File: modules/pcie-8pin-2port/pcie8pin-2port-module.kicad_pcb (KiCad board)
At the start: 4 copper layers, 105.7 x 66 mm, 24 parts, among them J1 RJ45_Amphenol_54602-x08_Horiz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, J5 USB_C_Receptacle_XKB_U262-16X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, SW1 Panasonic_EVQPUJ_EVQPUA, SW2 Panasonic_EVQPUJ_EVQPUA, U1 ESP32-S2-MINI-1, U10 VSSOP-10_3x3mm_P0.5mm, U11 VSSOP-10_3x3mm_P0.5mm, U2 SOIC-8_3.9x4.9mm_P1.27mm, U3 SOT-23-5

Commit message: PCIe: split into 2-port/3-port SKUs; generalize PCB gen; fix mount overlap
Per review: connectors were overlapping the corner mounts, and PCIe needs SKU
separation into a 2-port (4 connectors) and 3-port (6 connectors) board.

PCIe SKU separation:
- gen-modules.py SENSE/MODS now build pcie-8pin-2port (2 cables) and
  pcie-8pin-3port (3 cables); PINMAP keyed off the pcie base.
- modules/pcie-8pin renamed to modules/pcie-8pin-3port (git mv, history kept);
  new modules/pcie-8pin-2port added. Both schematics generated + audit-clean.

Generalized PCB floorplan generator (scripts/gen-module-pcb.py, replaces the
EPS-only gen-eps-pcb.py): parametric in cable count N. Generates EPS (2 cables,
~106x66), PCIe-2port (2, ~106x66) and PCIe-3port (3, ~133x66). N cables inline
(IN top / OUT bottom), cables INSET so the four corner M3 mounts clear the
connectors; shunts moved to mid-gap; the ESP + flash front end + RJ-45 vertically
separated on the right. Verified: 0 shorting_items on all three (was 8-10);
remaining DRC (~33 EPS / ~42 3-port) is silk/placement refinement for the GUI.

CLAUDE.md (board table, layout, generator bullet) + module READMEs updated.
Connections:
- J_IN1 pad 4: /SENSEC1_HI -> GND
- J_IN2 pad 4: /SENSEC2_HI -> GND
- J_OUT1 pad 4: /SENSEC1_LO -> GND
- J_OUT2 pad 4: /SENSEC2_LO -> GND
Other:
- board text added: "CEC pcie8pin-2port-module 4L 2oz/1oz"
- board text removed: "CEC eps8pin-module 4L 2oz/1oz"
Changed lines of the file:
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@@
 	)
 	(pad "4" thru_hole oval (at 12.6 0) (size 2.7 3.7) (drill 1.8) (layers "*.Cu" "*.Mask") (remove_unused_layers no)
-		(net 13 "/SENSEC1_HI")
+		(net 22 "GND")
 	)
 	(pad "5" thru_hole oval (at 0 5.5) (size 2.7 3.7) (drill 1.8) (layers "*.Cu" "*.Mask") (remove_unused_layers no)
@@
 	)
 	(pad "4" thru_hole oval (at 12.6 0) (size 2.7 3.7) (drill 1.8) (layers "*.Cu" "*.Mask") (remove_unused_layers no)
-		(net 14 "/SENSEC1_LO")
+		(net 22 "GND")
 	)
 	(pad "5" thru_hole oval (at 0 5.5) (size 2.7 3.7) (drill 1.8) (layers "*.Cu" "*.Mask") (remove_unused_layers no)
@@
 	)
 	(pad "4" thru_hole oval (at 12.6 0) (size 2.7 3.7) (drill 1.8) (layers "*.Cu" "*.Mask") (remove_unused_layers no)
-		(net 15 "/SENSEC2_HI")
+		(net 22 "GND")
 	)
 	(pad "5" thru_hole oval (at 0 5.5) (size 2.7 3.7) (drill 1.8) (layers "*.Cu" "*.Mask") (remove_unused_layers no)
@@
 	)
 	(pad "4" thru_hole oval (at 12.6 0) (size 2.7 3.7) (drill 1.8) (layers "*.Cu" "*.Mask") (remove_unused_layers no)
-		(net 16 "/SENSEC2_LO")
+		(net 22 "GND")
 	)
 	(pad "5" thru_hole oval (at 0 5.5) (size 2.7 3.7) (drill 1.8) (layers "*.Cu" "*.Mask") (remove_unused_layers no)
@@
 	(gr_line (start 105.7 66) (end 0 66) (stroke (width 0.1) (type solid)) (layer "Edge.Cuts"))
 	(gr_line (start 0 66) (end 0 0) (stroke (width 0.1) (type solid)) (layer "Edge.Cuts"))
-	(gr_text "CEC eps8pin-module  4L 2oz/1oz" (at 39.8 62 0) (layer "B.SilkS") (effects (font (size 0.9 0.9) (thickness 0.13)) (justify mirror)))
+	(gr_text "CEC pcie8pin-2port-module  4L 2oz/1oz" (at 39.8 62 0) (layer "B.SilkS") (effects (font (size 0.9 0.9) (thickness 0.13)) (justify mirror)))
 	(embedded_fonts no)
 )

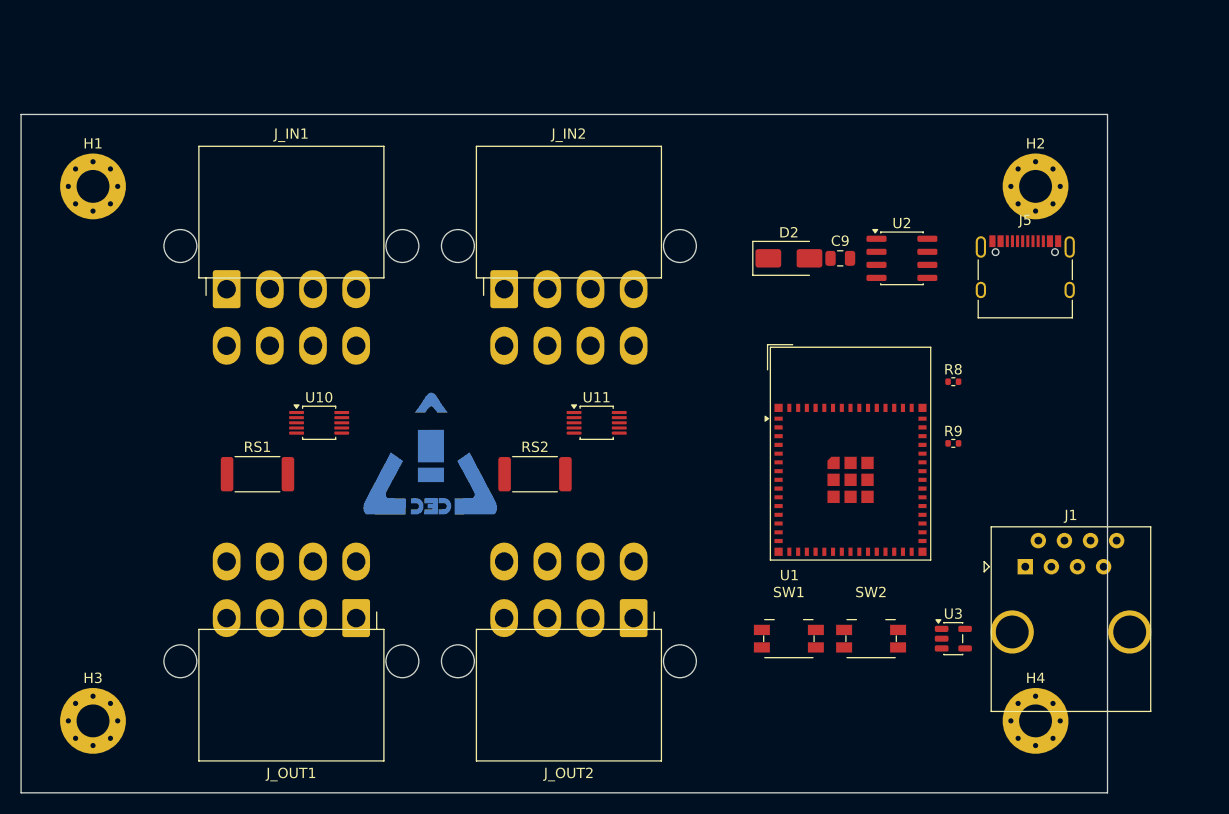
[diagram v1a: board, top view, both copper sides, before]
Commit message: Rotate USB-C + RJ-45 to mate outward on the right edge
Per review: the right-edge connectors (USB-C J5, RJ-45 J1) were mating downward
(+Y) instead of outward. Both footprints' openings face +Y at rotation 0, so
rotate them 90 (KiCad CCW, +Y -> +X) to mate out the right edge. The rotated
RJ-45 is ~18mm deep, so widen the electronics region (W = ex+40) and re-place
the core/flash around it; boards are now ~110x66 (EPS, PCIe-2port) and ~137x66
(PCIe-3port).

gen-module-pcb.py now bakes the footprint rotation into each pad's angle field
(KiCad convention). Without it, kicad-cli's headless DRC reported 25 FALSE
within-footprint pad shorts on the rotated USB-C (a known artifact, GUI-clean,
0 cross-part); with it, all three boards are back to 0 shorting_items,
0 clearance, 0 pth-in-courtyard (total DRC ~22 EPS / ~30 3-port, just silk).

CLAUDE.md + module READMEs updated (board sizes, connector orientation).
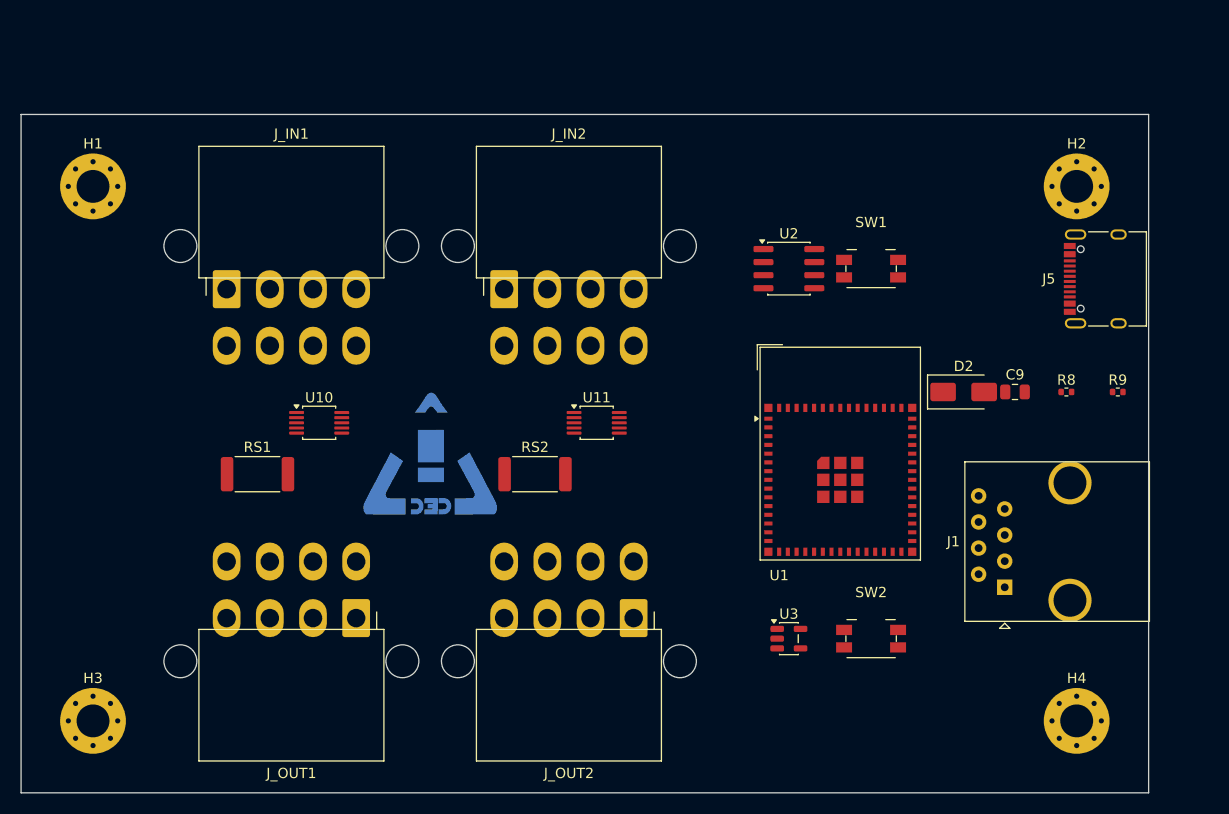
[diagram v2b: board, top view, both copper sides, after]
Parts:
- moved SW1 36.9 mm to (82.7, 15.0)
- moved C9 21.4 mm to (96.7, 27.0)
- moved D2 21.4 mm to (91.7, 27.0)
- moved R9 16.8 mm to (106.7, 27.0)
- moved U3 16.0 mm to (74.7, 51.0)
- moved R8 11.0 mm to (101.7, 27.0)
- moved U2 11.0 mm to (74.7, 15.0)
- moved J5 8.00 mm to (105.7, 16.0), turned to 90 degrees
- moved H2 4.00 mm to (102.7, 7.00)
- moved H4 4.00 mm to (102.7, 59.0)
- moved J1 2.83 mm to (95.7, 46.0), turned to 90 degrees
- moved U1 1.00 mm to (79.7, 33.0)
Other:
- board size 105.7 x 66 mm -> 109.7 x 66 mm

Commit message: 12VHPWR Standard: add INA240 input RC filter, sideband sense taps, tighten board + values-on-silk
Schematic (gen-modules.py, analog-pin topology):
- INA240 input anti-alias/transient RC filter per channel: matched 10 ohm series
  Rf on each input (RFH/RFL1-6) + 470 nF differential cap (CF1-6).
  fc = 1/(2*pi*2*Rf*Cdiff) ~= 16.9 kHz, so the ~10 kHz GPU transients pass at
  ~-1.3 dB and HF rolls off ahead of the ESP32-S3 ADC. Rf held at 10 ohm + matched
  (TI's INA240 ceiling) for negligible gain/CMRR error.
- The four 12V-2x6 sideband sense pins (13-16: SENSE0/SENSE1/CARD_PWR_STABLE/
  CARD_CBL_PRES#) now pass through J3->J4 AND each taps a free ESP32-S3 GPIO
  (IO8/9/11/12) via a 1k series R (R10-R13) so firmware can read the cable's
  advertised power capability + present/stable state and report over CAN.
- Moved the I2C pull-ups R3/R4 into the i2c-only branch (they were unused/floating
  on the analog module) to free IO8/IO9 for two of the sideband taps.
- footprint_for: 470n -> C_0603. ERC clean; netlist verified.

PCB floorplan (gen-module-pcb.py):
- Values-on-silk pass (all boards): place() rewrites each part's Value property to
  the netlist value and moves it from the non-plotted F.Fab to F.SilkS so values
  are readable on the board; mounts/logo keep their Fab default.
- 12VHPWR tightened 46x104 -> 44x92 with plug connectors overhanging their edge:
  J3's right-angle shroud overhangs the TOP edge (~3mm, pads ~6.5mm in), J1/J5
  overhang the RIGHT edge; J4 keeps J3's rotation so the six +12V lanes stay
  straight + equal-length (melt prevention). Shunt rows spaced 8mm (rotated 2512
  is 6.3mm tall), mounts moved above/below the 14mm ESP.
- DRC: 0 structural hits (0 copper shorts / clearance / courtyard / copper-edge);
  remaining is silk (values-on-silk + tight placement) + known lib_footprint_mismatch.

Docs: README + CLAUDE.md updated to match.
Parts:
- C9: value C_0805_2012Metric -> 10uF
- D2: value D_SMA -> SS34
- J1: value RJ45_Amphenol_54602-x08_Horizontal -> TO-HUB
- J5: value USB_C_Receptacle_XKB_U262-16XN-4BVC11 -> USB-C 2.0
- J_IN1: value Molex_Mini-Fit_Jr_5569-08A2_2x04_P4.20mm_Horizontal -> C1 PSU
- J_IN2: value Molex_Mini-Fit_Jr_5569-08A2_2x04_P4.20mm_Horizontal -> C2 PSU
- J_OUT1: value Molex_Mini-Fit_Jr_5569-08A2_2x04_P4.20mm_Horizontal -> C1 LOAD
- J_OUT2: value Molex_Mini-Fit_Jr_5569-08A2_2x04_P4.20mm_Horizontal -> C2 LOAD
- R8, R9: value R_0402_1005Metric -> 5.1kΩ
- RS1, RS2: value R_2512_6332Metric -> 0.5mΩ
- SW1: value Panasonic_EVQPUJ_EVQPUA -> BOOT
- SW2: value Panasonic_EVQPUJ_EVQPUA -> RESET
- U1: value ESP32-S2-MINI-1 -> ESP32-S3-MINI-1-N4R2
- U10, U11: value VSSOP-10_3x3mm_P0.5mm -> INA238
- U2: value SOIC-8_3.9x4.9mm_P1.27mm -> TJA1462A
- U3: value SOT-23-5 -> LP5907MFX-3.3
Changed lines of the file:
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@@
 		(effects (font (size 1 1) (thickness 0.15)))
 	)
-	(property "Value" "Molex_Mini-Fit_Jr_5569-08A2_2x04_P4.20mm_Horizontal"
+	(property "Value" "C1 PSU"
 		(at 6.3 8.55 0)
-		(layer "F.Fab")
+		(layer "F.SilkS")
 		(effects (font (size 1 1) (thickness 0.15)))
 	)
@@
 		(effects (font (size 1 1) (thickness 0.15)))
 	)
-	(property "Value" "Molex_Mini-Fit_Jr_5569-08A2_2x04_P4.20mm_Horizontal"
+	(property "Value" "C1 LOAD"
 		(at 6.3 8.55 0)
-		(layer "F.Fab")
+		(layer "F.SilkS")
 		(effects (font (size 1 1) (thickness 0.15)))
 	)
@@
 		)
 	)
-	(property "Value" "R_2512_6332Metric"
+	(property "Value" "0.5mΩ"
 		(at 0 2.63 0)
-		(layer "F.Fab")
+		(layer "F.SilkS")
 		(effects
 			(font
@@
 		)
 	)
-	(property "Value" "VSSOP-10_3x3mm_P0.5mm"
+	(property "Value" "INA238"
 		(at 0 2.45 0)
-		(layer "F.Fab")
+		(layer "F.SilkS")
 		(effects
 			(font
@@
 		(effects (font (size 1 1) (thickness 0.15)))
 	)
-	(property "Value" "Molex_Mini-Fit_Jr_5569-08A2_2x04_P4.20mm_Horizontal"
+	(property "Value" "C2 PSU"
 		(at 6.3 8.55 0)
-		(layer "F.Fab")
+		(layer "F.SilkS")
 		(effects (font (size 1 1) (thickness 0.15)))
 	)
@@
 		(effects (font (size 1 1) (thickness 0.15)))
 	)
-	(property "Value" "Molex_Mini-Fit_Jr_5569-08A2_2x04_P4.20mm_Horizontal"
+	(property "Value" "C2 LOAD"
 		(at 6.3 8.55 0)
-		(layer "F.Fab")
+		(layer "F.SilkS")
 		(effects (font (size 1 1) (thickness 0.15)))
 	)
@@
 		)
 	)
-	(property "Value" "R_2512_6332Metric"
+	(property "Value" "0.5mΩ"
 		(at 0 2.63 0)
-		(layer "F.Fab")
+		(layer "F.SilkS")
 		(effects
 			(font
@@
 		)
 	)
-	(property "Value" "VSSOP-10_3x3mm_P0.5mm"
+	(property "Value" "INA238"
 		(at 0 2.45 0)
-		(layer "F.Fab")
+		(layer "F.SilkS")
 		(effects
 			(font
@@
 		)
 	)
-	(property "Value" "ESP32-S2-MINI-1"
+	(property "Value" "ESP32-S3-MINI-1-N4R2"
 		(at 0 3.55 0)
 		(unlocked yes)
-		(layer "F.Fab")
+		(layer "F.SilkS")
 		(effects
 			(font
@@
 		)
 	)
-	(property "Value" "SOIC-8_3.9x4.9mm_P1.27mm"
+	(property "Value" "TJA1462A"
 		(at 0 3.4 0)
-		(layer "F.Fab")
+		(layer "F.SilkS")
 		(effects
 			(font
@@
 		)
 	)
-	(property "Value" "SOT-23-5"
+	(property "Value" "LP5907MFX-3.3"
 		(at 0 2.4 0)
-		(layer "F.Fab")
+		(layer "F.SilkS")
 		(effects
 			(font
@@
 		)
 	)
-	(property "Value" "Panasonic_EVQPUJ_EVQPUA"
+	(property "Value" "BOOT"
 		(at 0 3.5 0)
-		(layer "F.Fab")
+		(layer "F.SilkS")
 		(effects
 			(font
@@
 		)
 	)
-	(property "Value" "Panasonic_EVQPUJ_EVQPUA"
+	(property "Value" "RESET"
 		(at 0 3.5 0)
-		(layer "F.Fab")
+		(layer "F.SilkS")
 		(effects
 			(font
@@
 		)
 	)
-	(property "Value" "D_SMA"
+	(property "Value" "SS34"
 		(at 0 2.6 0)
-		(layer "F.Fab")
+		(layer "F.SilkS")
 		(effects
 			(font
@@
 		)
 	)
-	(property "Value" "C_0805_2012Metric"
+	(property "Value" "10uF"
 		(at 0 1.68 0)
-		(layer "F.Fab")
+		(layer "F.SilkS")
 		(effects
 			(font
@@
 		)
 	)
-	(property "Value" "R_0402_1005Metric"
+	(property "Value" "5.1kΩ"
 		(at 0 1.17 0)
-		(layer "F.Fab")
+		(layer "F.SilkS")
 		(effects
 			(font
@@
 		)
 	)
-	(property "Value" "R_0402_1005Metric"
+	(property "Value" "5.1kΩ"
 		(at 0 1.17 0)
-		(layer "F.Fab")
+		(layer "F.SilkS")
 		(effects
 			(font
@@
 		)
 	)
-	(property "Value" "USB_C_Receptacle_XKB_U262-16XN-4BVC11"
+	(property "Value" "USB-C 2.0"
 		(at 0 4.935 0)
-		(layer "F.Fab")
+		(layer "F.SilkS")
 		(effects
 			(font
@@
 		)
 	)
-	(property "Value" "RJ45_Amphenol_54602-x08_Horizontal"
+	(property "Value" "TO-HUB"
 		(at 4.445 4 0)
-		(layer "F.Fab")
+		(layer "F.SilkS")
 		(effects
 			(font
